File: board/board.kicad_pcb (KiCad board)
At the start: 2 copper layers, 37 x 29 mm, 26 parts, among them J1 013_PoE_rectified, J2 003_power, U1 MP8007, U2 POE70P-50L

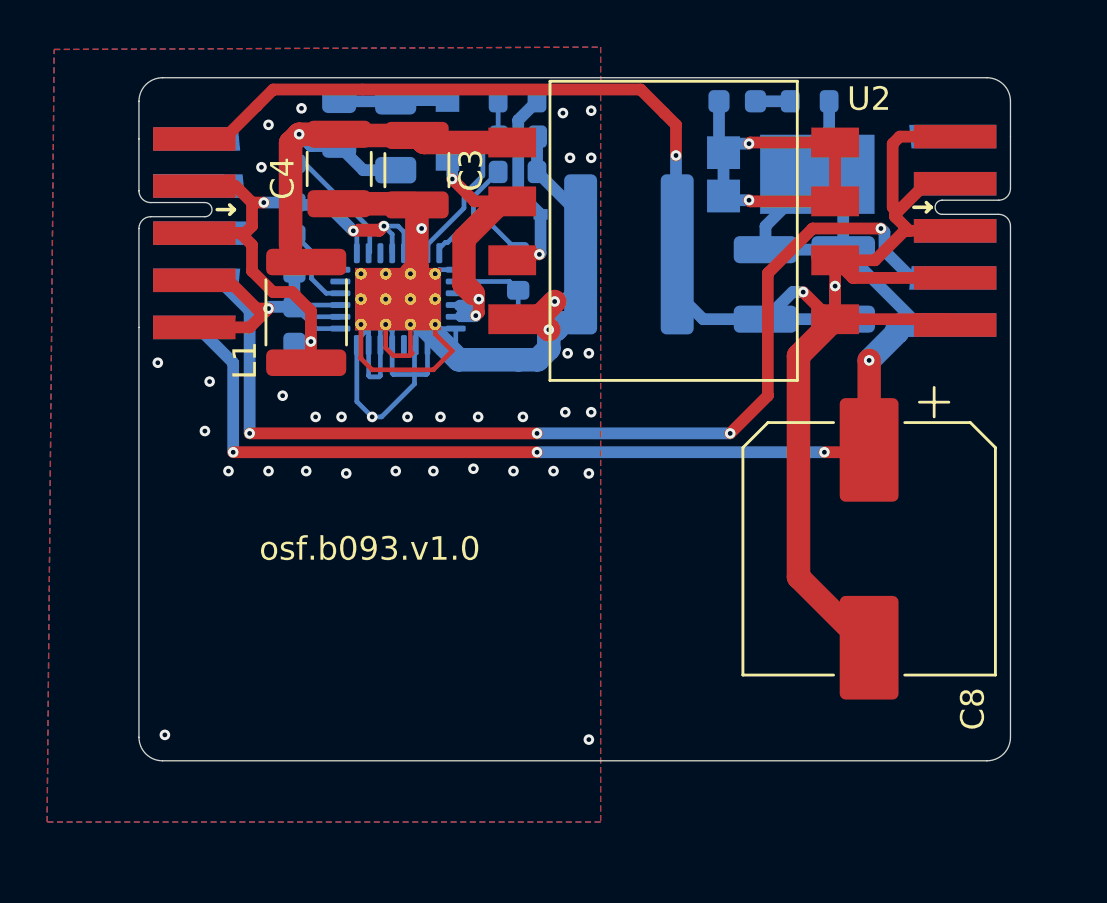
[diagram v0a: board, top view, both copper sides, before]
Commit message: improved thermal properties of layout
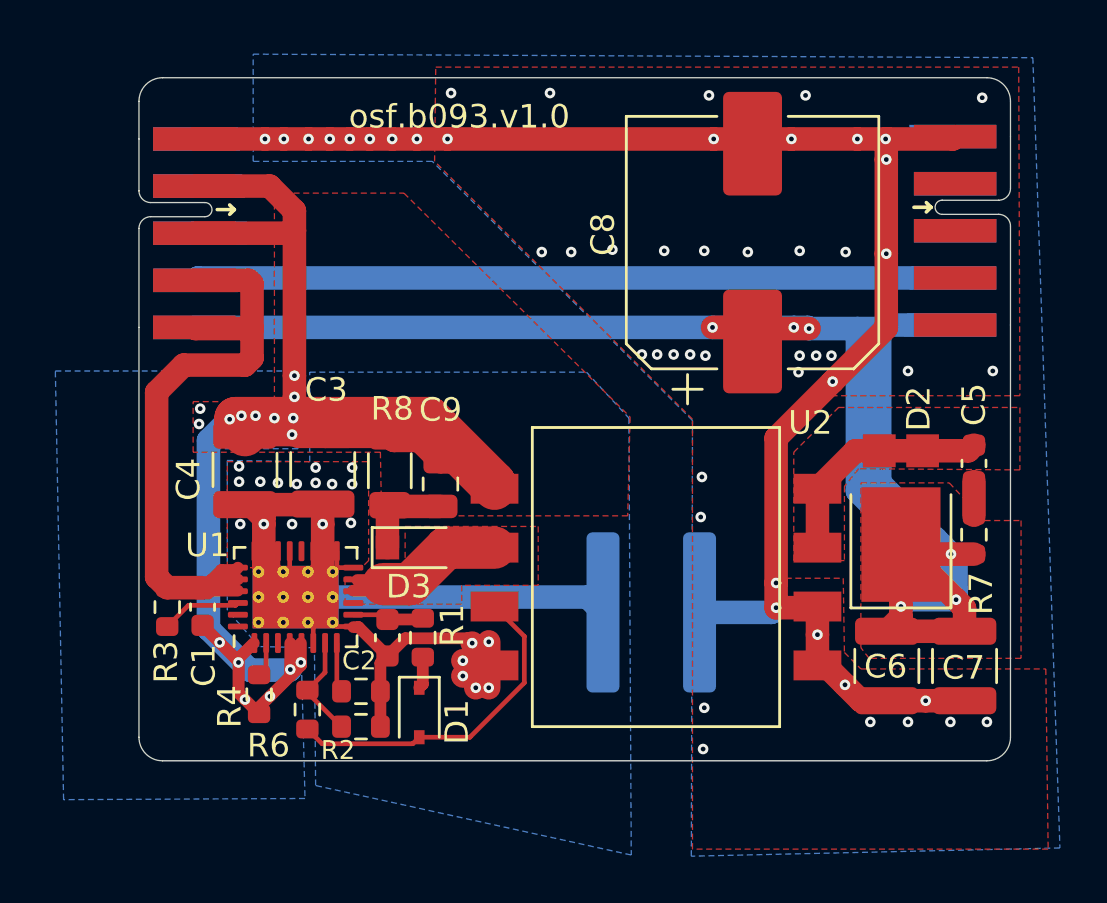
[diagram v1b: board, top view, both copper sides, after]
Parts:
- removed L1: 0R, Inductor_SMD:L_1812_4532Metric
- C1, C2, C5, C6, C7, C9, D1, D2, D3, R2, R3, R4, R5, R7, R8, U1: moved to F.Cu
- R1: value 2.2k -> 5.1k; moved to F.Cu
- R6: value 105k -> 110k; moved to F.Cu
- moved R6 27.3 mm to (84.2, 100.8), turned to 90 degrees
- moved R2 25.9 mm to (86.4, 101.5)
- moved R5 23.0 mm to (86.4, 100.0)
- moved R4 21.8 mm to (82.1, 100.2)
- moved D1 21.5 mm to (88.9, 101.0), turned to -90 degrees
- moved R7 19.7 mm to (112.5, 93.4), turned to 90 degrees
- moved C5 18.4 mm to (112.5, 90.4), turned to -90 degrees
- moved C7 18.3 mm to (112.0, 99.0)
- moved D3 17.8 mm to (88.8, 94.0), turned to 0 degrees
- moved C6 16.3 mm to (108.8, 99.0)
- moved R1 16.1 mm to (89.0, 97.8), turned to 90 degrees
- moved R3 15.9 mm to (78.2, 96.5), turned to 90 degrees
- moved C9 15.9 mm to (89.8, 91.2), turned to -90 degrees
- moved D2 15.3 mm to (109.3, 92.7), turned to 90 degrees
- moved C10 15.2 mm to (98.8, 96.7)
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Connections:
- net Net-(C2-Pad1) renamed /flyback/VCC
- net Net-(C5-Pad1) renamed /flyback/transformer_out
- net Net-(D3-Pad2) renamed /flyback/SW
- net Net-(R2-Pad1) renamed /flyback/FB1
- C3 pad 1: Net-(C3-Pad1) -> /flyback/PoE+
- C4 pad 1: Net-(C3-Pad1) -> /flyback/PoE+
- C9 pad 1: Net-(C3-Pad1) -> /flyback/PoE+
- J2 pad 2: GND -> unconnected-(J2-Pad2)
- J2 pad 3: GND -> unconnected-(J2-Pad3)
- J2 pad 4: GND -> unconnected-(J2-Pad4)
- J2 pad 5: GND -> unconnected-(J2-Pad5)
- R8 pad 2: Net-(C3-Pad1) -> /flyback/PoE+
- U2 pad 4: Net-(C3-Pad1) -> /flyback/PoE+
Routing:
- net /flyback/PoE+: track 28.2 -> 72.5 mm, vias 4 -> 16
- net /5V: track 61.5 -> 90.3 mm, vias 4 -> 6
- net Net-(C3-Pad1): track 19.8 -> 0.00 mm, vias 1 -> 0
- net GND: track 86.2 -> 68.7 mm, vias 3 -> 53
- net /flyback/GNDPWR: track 72.2 -> 56.0 mm, vias 37 -> 21
- net /3.3V: track 45.9 -> 32.2 mm, vias 4 -> 0
- net /flyback/PoE-: track 16.1 -> 27.8 mm, vias 1 -> 0
- net /flyback/transformer_out: track 16.3 -> 9.91 mm, vias 2 -> 0
- net Net-(D1-Pad2): track 8.50 -> 14.3 mm, vias 1 -> 0
- net Net-(R4-Pad2): track 5.41 -> 1.47 mm
- net /flyback/FB1: track 7.79 -> 4.46 mm
- net Net-(R5-Pad1): track 4.54 -> 2.13 mm
- net /flyback/VCC: track 4.21 -> 3.05 mm
- net Net-(D1-Pad1): track 2.05 -> 1.36 mm
- net Net-(C9-Pad2): track 4.62 -> 4.01 mm
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- added copper zone on F.Cu, net /5V
- added copper zone on B.Cu, net /flyback/PoE+
- added copper zone on F.Cu, net /flyback/PoE+
- added copper zone on F.Cu, net /flyback/SW
- added copper zone on F.Cu, net /flyback/transformer_out
- added copper zone on B.Cu, net GND
- added copper zone on F.Cu, net GND

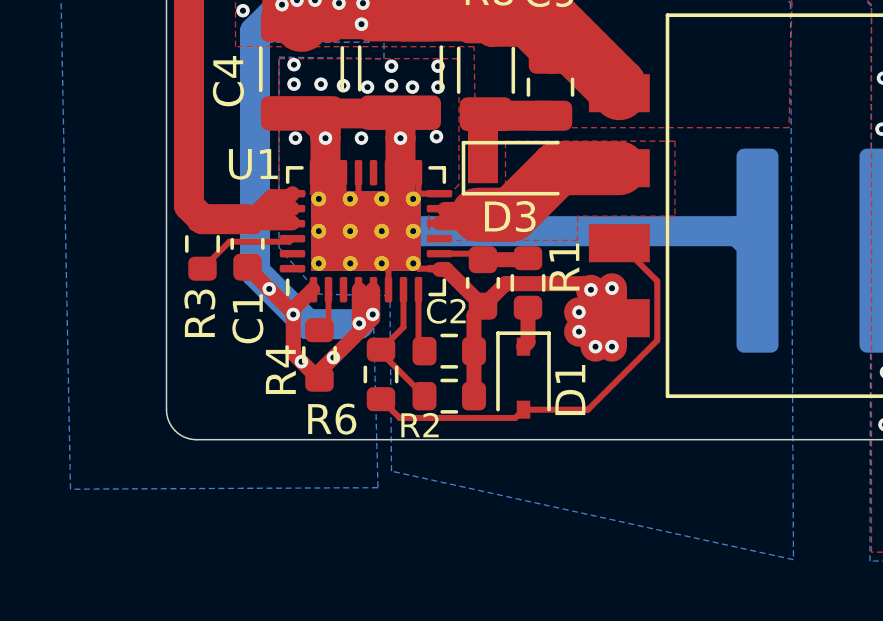
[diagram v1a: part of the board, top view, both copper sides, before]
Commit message: updated voltage and current setting resistors
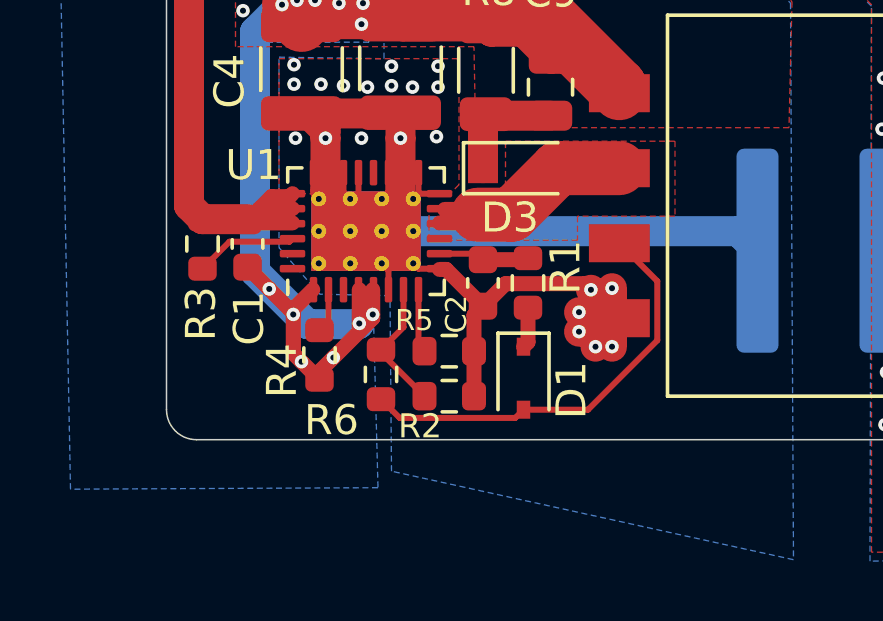
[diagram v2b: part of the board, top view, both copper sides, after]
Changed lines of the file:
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@@
     (property "Sheetname" "flyback")
     (attr smd)
-    (fp_text reference "C2" (at 0.975 1.2 180) (layer "F.SilkS")
-      (effects (font (size 0.8 0.8) (thickness 0.15)))
+    (fp_text reference "C2" (at 1.045 0.89 -90) (layer "F.SilkS")
+      (effects (font (size 0.7 0.7) (thickness 0.15)))
     )
     (fp_text value "1uF" (at 0 1.43 90) (layer "F.Fab")
@@
     (property "Sheetname" "flyback")
     (attr smd)
-    (fp_text reference "R5" (at -0.175 -1.65) (layer "B.SilkS")
-      (effects (font (size 1 1) (thickness 0.15)) (justify mirror))
+    (fp_text reference "R5" (at -1.165 -1.03) (layer "F.SilkS")
+      (effects (font (size 0.7 0.7) (thickness 0.15)))
     )
     (fp_text value "49.9k" (at 0.225 1.7) (layer "B.Fab")
